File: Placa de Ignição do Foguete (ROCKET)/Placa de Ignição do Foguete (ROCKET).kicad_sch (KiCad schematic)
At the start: 1 part, among them U1 ESP32-DEVKITC-32E

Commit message: ESP, LoRa e circuito Mosfet
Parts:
- added J1: Bateria ESP, symbol Connector:Screw_Terminal_01x02
- added J2: Bateria Squibs, symbol Connector:Screw_Terminal_01x02
- added J3: Squibs (Out), symbol Connector:Screw_Terminal_01x02
- added Q1: Q_NMOS_GDS, symbol Transistor_FET:Q_NMOS_GDS
- added R1: 330, symbol Device:R
- added R2: 10k, symbol Device:R
- added U2: RA-02_LORA, Meus_Footprints:MODULE_RA-02_LORA, symbol RA-02_LORA:RA-02_LORA
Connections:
- net 3V3: now reaches U1.J2_1 (3V3)
- net 3V3: now also U2.3 (3.3V)
- net RST (LoRa): now reaches U1.J2_12 (IO14)
- net RST (LoRa): now also U2.4 (RESET)
- net GND: now reaches U1.J2_14 (GND_J2_14)
- net GND: now also U1.J3_1 (GND_J3_1), U1.J3_7 (GND_J3_7), J1.2 (Pin_2), J2.2 (Pin_2), Q1.3 (S), R2.2, U2.1 (GND), U2.16 (GND), U2.2 (GND), U2.9 (GND)
- net VCC (ESP): now reaches U1.J2_19 (EXT_5V)
- net VCC (ESP): now also J1.1 (Pin_1)
- net NSS / CS (LoRa): now reaches U1.J3_10 (IO5)
- net NSS / CS (LoRa): now also U2.15 (NSS)
- net DIO0 (LoRa): now reaches U1.J3_15 (IO2)
- net DIO0 (LoRa): now also U2.5 (DI00)
- net GATE_CTRL: now reaches U1.J3_16 (IO15)
- net GATE_CTRL: now also R1.1
- net MOSI (LoRa): now reaches U1.J3_2 (IO23)
- net MOSI (LoRa): now also U2.14 (MOSI)
- net MISO (LoRa): now reaches U1.J3_8 (IO19)
- net MISO (LoRa): now also U2.13 (MISO)
- net SCK (LoRa): now reaches U1.J3_9 (IO18)
- net SCK (LoRa): now also U2.12 (SCK)
- new net: Q1.1 (G), R1.2, R2.1
- new net GND Squibes (Out): J3.2 (Pin_2), Q1.2 (D)
- new net VCC_SQUIB: J2.1 (Pin_1), J3.1 (Pin_1)
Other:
- moved on the sheet: U1

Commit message: Teste rapido
Pode dar cagada
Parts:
- U1: footprint Meus_Footprints:MODULE_ESP32-DEVKITC-32E -> Footprints:MODULE_ESP32-DEVKITC-32E
- U2: footprint Meus_Footprints:MODULE_RA-02_LORA -> Footprints:MODULE_RA-02_LORA
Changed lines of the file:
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@@
 			)
 		)
-		(property "Footprint" "Meus_Footprints:MODULE_RA-02_LORA"
+		(property "Footprint" "Footprints:MODULE_RA-02_LORA"
 			(at 218.44 87.63 0)
 			(show_name no)
@@
 			)
 		)
-		(property "Footprint" "Meus_Footprints:MODULE_ESP32-DEVKITC-32E"
+		(property "Footprint" "Footprints:MODULE_ESP32-DEVKITC-32E"
 			(at 120.65 100.33 0)
 			(hide yes)

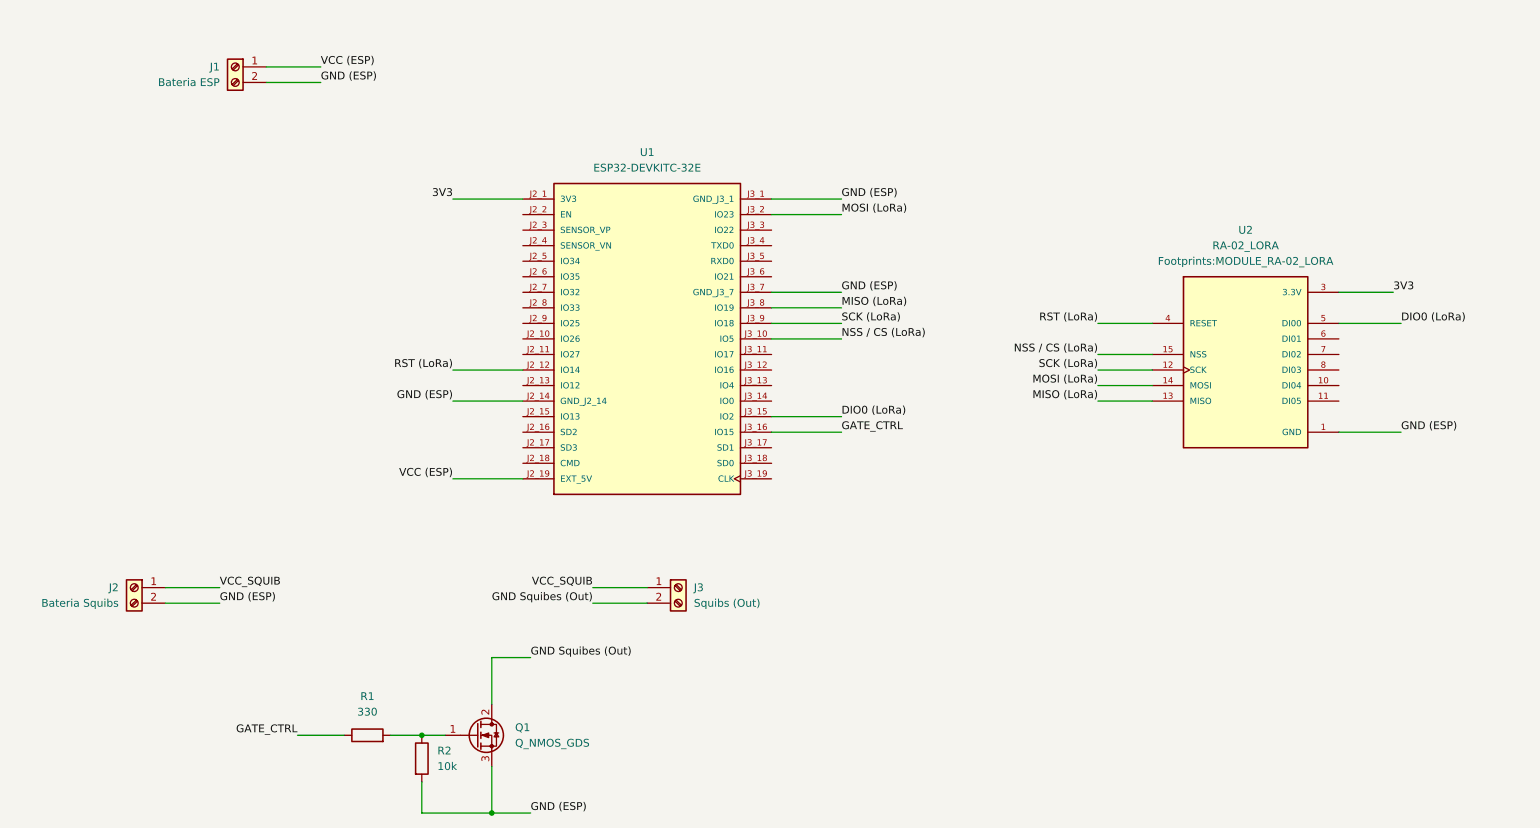
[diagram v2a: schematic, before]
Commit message: Correção de problemas com os squibes
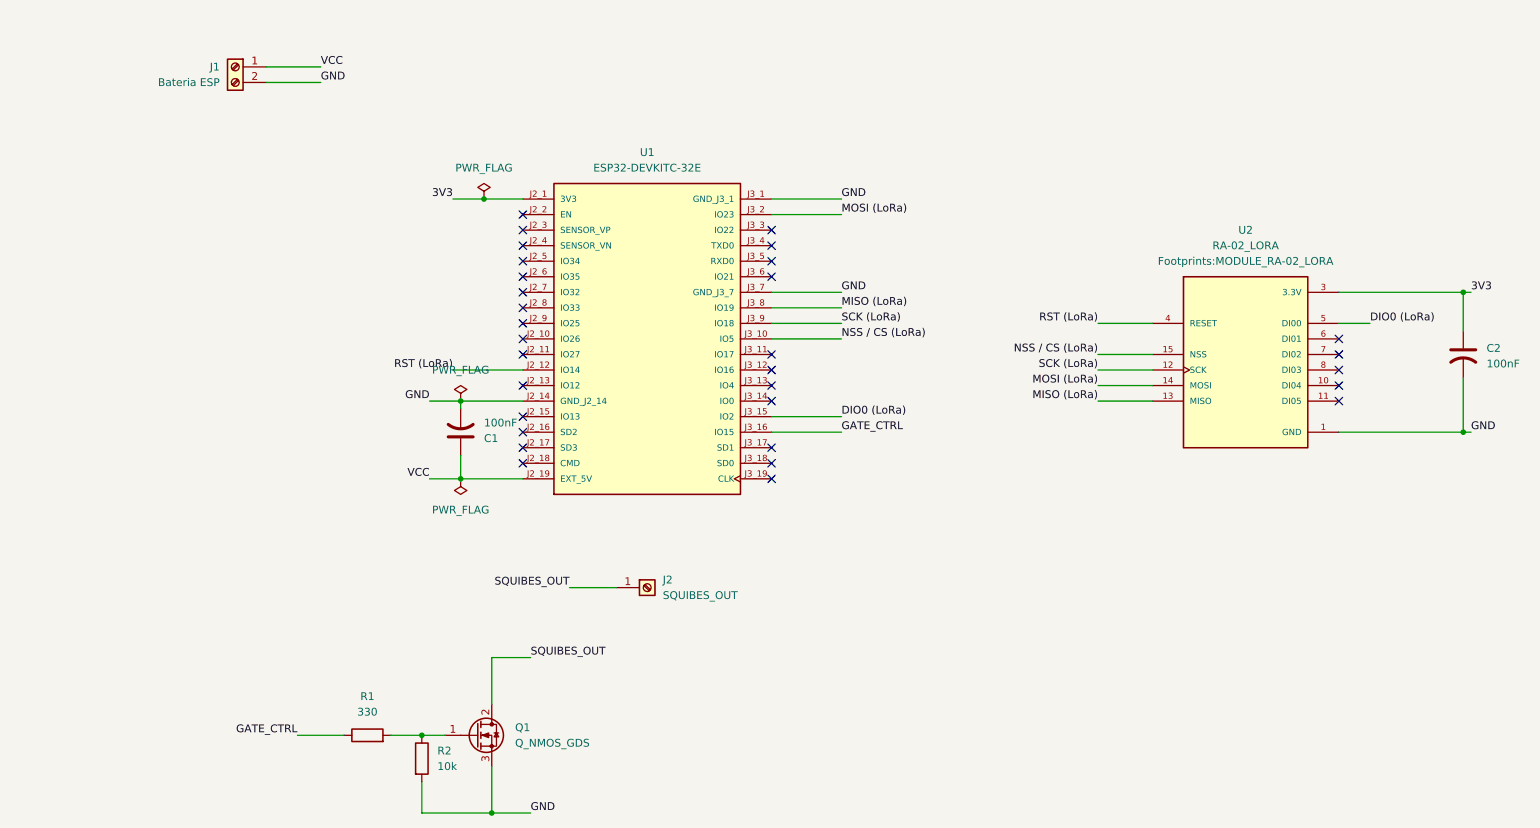
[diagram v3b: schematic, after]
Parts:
- removed J2: Bateria Squibs, symbol Connector:Screw_Terminal_01x02
- removed J3: Squibs (Out), symbol Connector:Screw_Terminal_01x02
- added C1, C2: 100nF, symbol Device:C_US
- added J2: SQUIBES_OUT, symbol Connector:Screw_Terminal_01x01
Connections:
- net 3V3: now also C2.1
- net GND: now also C1.2, C2.2
- net GND Squibes (Out) renamed SQUIBES_OUT
- net SQUIBES_OUT: now also J2.1 (Pin_1)
- net VCC (ESP) renamed VCC
- net VCC: now also C1.1
- no-connect marks 0 -> 31

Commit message: Tentativa inicial de Trilhas lógicas e de alimentação
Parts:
- removed J2: SQUIBES_OUT, symbol Connector:Screw_Terminal_01x01
- added J3: Squibes, TerminalBlock_Phoenix:TerminalBlock_Phoenix_MKDS-1,5-2-5.08_1x02_P5.08mm_Horizontal, symbol Connector:Screw_Terminal_01x02
- C1, C2: footprint (none) -> Capacitor_THT:C_Disc_D5.0mm_W2.5mm_P5.00mm
- J1: footprint (none) -> TerminalBlock_Phoenix:TerminalBlock_Phoenix_MKDS-1,5-2-5.08_1x02_P5.08mm_Horizontal
- Q1: footprint (none) -> Package_TO_SOT_THT:TO-220-3_Vertical
- R1: footprint (none) -> Resistor_THT:R_Axial_DIN0207_L6.3mm_D2.5mm_P7.62mm_Horizontal
- R2: value 10k -> 100k; footprint (none) -> Resistor_THT:R_Axial_DIN0207_L6.3mm_D2.5mm_P7.62mm_Horizontal
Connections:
- net SQUIBES_OUT: now also J3.2 (Pin_2)
- net VCC: now also J3.1 (Pin_1)
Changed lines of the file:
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@@
 	(wire
 		(pts
-			(xy 88.9 105.41) (xy 100.33 105.41)
+			(xy 90.17 102.87) (xy 97.79 102.87)
 		)
 		(stroke
@@
 	(wire
 		(pts
+			(xy 97.79 105.41) (xy 100.33 105.41)
+		)
+		(stroke
+			(width 0)
+			(type default)
+		)
+	)
+	(wire
+		(pts
+			(xy 114.3 148.59) (xy 124.46 148.59)
+		)
+		(stroke
+			(width 0)
+			(type default)
+		)
+	)
+	(wire
+		(pts
 			(xy 83.82 165.1) (xy 78.74 165.1)
 		)
@@
 	(wire
 		(pts
+			(xy 114.3 146.05) (xy 124.46 146.05)
+		)
+		(stroke
+			(width 0)
+			(type default)
+		)
+	)
+	(wire
+		(pts
 			(xy 233.68 97.79) (xy 238.76 97.79)
 		)
@@
 	(wire
 		(pts
+			(xy 97.79 102.87) (xy 97.79 105.41)
+		)
+		(stroke
+			(width 0)
+			(type default)
+		)
+	)
+	(wire
+		(pts
 			(xy 140.97 92.71) (xy 152.4 92.71)
 		)
@@
 		(pts
 			(xy 194.31 107.95) (xy 203.2 107.95)
-		)
-		(stroke
-			(width 0)
-			(type default)
-		)
-	)
-	(wire
-		(pts
-			(xy 107.95 140.97) (xy 115.57 140.97)
 		)
 		(stroke
@@
 		)
 	)
+	(label "SQUIBES_OUT"
+		(at 114.3 148.59 180)
+		(effects
+			(font
+				(size 1.27 1.27)
+			)
+			(justify right bottom)
+		)
+	)
 	(label "DIO0 (LoRa)"
 		(at 238.76 97.79 0)
@@
 		)
 	)
-	(label "SQUIBES_OUT"
-		(at 107.95 140.97 180)
-		(effects
-			(font
-				(size 1.27 1.27)
-			)
-			(justify right bottom)
-		)
-	)
 	(label "MOSI (LoRa)"
 		(at 152.4 80.01 0)
@@
 		)
 	)
+	(label "VCC"
+		(at 114.3 146.05 180)
+		(effects
+			(font
+				(size 1.27 1.27)
+			)
+			(justify right bottom)
+		)
+	)
 	(label "GATE_CTRL"
 		(at 152.4 115.57 0)
@@
 	)
 	(label "RST (LoRa)"
-		(at 88.9 105.41 180)
+		(at 90.17 102.87 180)
 		(effects
 			(font
@@
 			)
 		)
-		(property "Footprint" ""
+		(property "Footprint" "Resistor_THT:R_Axial_DIN0207_L6.3mm_D2.5mm_P7.62mm_Horizontal"
 			(at 74.93 166.878 90)
 			(hide yes)
@@
 				(path "/26d3337e-e27e-417f-84cb-6b82cf1162f8"
 					(reference "R1")
-					(unit 1)
-				)
-			)
-		)
-	)
-	(symbol
-		(lib_id "Connector:Screw_Terminal_01x01")
-		(at 120.65 140.97 0)
-		(unit 1)
-		(body_style 1)
-		(exclude_from_sim no)
-		(in_bom yes)
-		(on_board yes)
-		(in_pos_files yes)
-		(dnp no)
-		(fields_autoplaced yes)
-		(property "Reference" "J2"
-			(at 123.19 139.6999 0)
-			(show_name no)
-			(do_not_autoplace no)
-			(effects
-				(font
-					(size 1.27 1.27)
-				)
-				(justify left)
-			)
-		)
-		(property "Value" "SQUIBES_OUT"
-			(at 123.19 142.2399 0)
-			(show_name no)
-			(do_not_autoplace no)
-			(effects
-				(font
-					(size 1.27 1.27)
-				)
-				(justify left)
-			)
-		)
-		(property "Footprint" ""
-			(at 120.65 140.97 0)
-			(hide yes)
-			(show_name no)
-			(do_not_autoplace no)
-			(effects
-				(font
-					(size 1.27 1.27)
-				)
-			)
-		)
-		(property "Datasheet" ""
-			(at 120.65 140.97 0)
-			(hide yes)
-			(show_name no)
-			(do_not_autoplace no)
-			(effects
-				(font
-					(size 1.27 1.27)
-				)
-			)
-		)
-		(property "Description" "Generic screw terminal, single row, 01x01, script generated (kicad-library-utils/schlib/autogen/connector/)"
-			(at 120.65 140.97 0)
-			(hide yes)
-			(show_name no)
-			(do_not_autoplace no)
-			(effects
-				(font
-					(size 1.27 1.27)
-				)
-			)
-		)
-		(pin "1"
-		)
-		(instances
-			(project "Placa de Ignição do Foguete (ROCKET)"
-				(path "/26d3337e-e27e-417f-84cb-6b82cf1162f8"
-					(reference "J2")
 					(unit 1)
 				)
@@
 			)
 		)
-		(property "Footprint" ""
+		(property "Footprint" "Capacitor_THT:C_Disc_D5.0mm_W2.5mm_P5.00mm"
 			(at 254 102.87 0)
 			(hide yes)
@@
 			)
 		)
-		(property "Footprint" ""
+		(property "Footprint" "Package_TO_SOT_THT:TO-220-3_Vertical"
 			(at 97.79 162.56 0)
 			(hide yes)
@@
 			)
 		)
-		(property "Footprint" ""
+		(property "Footprint" "Capacitor_THT:C_Disc_D5.0mm_W2.5mm_P5.00mm"
 			(at 90.17 115.57 0)
 			(hide yes)
@@
 			)
 		)
-		(property "Value" "10k"
+		(property "Value" "100k"
 			(at 86.36 170.1799 0)
 			(show_name no)
@@
 			)
 		)
-		(property "Footprint" ""
+		(property "Footprint" "Resistor_THT:R_Axial_DIN0207_L6.3mm_D2.5mm_P7.62mm_Horizontal"
 			(at 82.042 168.91 90)
 			(hide yes)
@@
 			)
 		)
-		(property "Footprint" ""
+		(property "Footprint" "TerminalBlock_Phoenix:TerminalBlock_Phoenix_MKDS-1,5-2-5.08_1x02_P5.08mm_Horizontal"
 			(at 53.34 55.88 0)
 			(hide yes)
@@
 					(unit 1)
 				)
+			)
+		)
+	)
+	(symbol
+		(lib_name "Screw_Terminal_01x02_1")
+		(lib_id "Connector:Screw_Terminal_01x02")
+		(at 129.54 146.05 0)
+		(unit 1)
+		(body_style 1)
+		(exclude_from_sim no)
+		(in_bom yes)
+		(on_board yes)
+		(in_pos_files yes)
+		(dnp no)
+		(fields_autoplaced yes)
+		(property "Reference" "J3"
+			(at 132.08 146.0499 0)
+			(show_name no)
+			(do_not_autoplace no)
+			(effects
+				(font
+					(size 1.27 1.27)
+				)
+				(justify left)
+			)
+		)
+		(property "Value" "Squibes"
+			(at 132.08 148.5899 0)
+			(show_name no)
+			(do_not_autoplace no)
+			(effects
+				(font
+					(size 1.27 1.27)
+				)
+				(justify left)
+			)
+		)
+		(property "Footprint" "TerminalBlock_Phoenix:TerminalBlock_Phoenix_MKDS-1,5-2-5.08_1x02_P5.08mm_Horizontal"
+			(at 129.54 146.05 0)
+			(hide yes)
+			(show_name no)
+			(do_not_autoplace no)
+			(effects
+				(font
+					(size 1.27 1.27)
+				)
+			)
+		)
+		(property "Datasheet" ""
+			(at 129.54 146.05 0)
+			(hide yes)
+			(show_name no)
+			(do_not_autoplace no)
+			(effects
+				(font
+					(size 1.27 1.27)
+				)
+			)
+		)
+		(property "Description" "Generic screw terminal, single row, 01x02, script generated (kicad-library-utils/schlib/autogen/connector/)"
+			(at 129.54 146.05 0)
+			(hide yes)
+			(show_name no)
+			(do_not_autoplace no)
+			(effects
+				(font
+					(size 1.27 1.27)
+				)
+			)
+		)
+		(pin "1"
+		)
+		(pin "2"
+		)
+		(instances
+			(project "Placa de Ignição do Foguete (ROCKET)"
+				(path "/26d3337e-e27e-417f-84cb-6b82cf1162f8"
+					(reference "J3")
+					(unit 1)
+				)
